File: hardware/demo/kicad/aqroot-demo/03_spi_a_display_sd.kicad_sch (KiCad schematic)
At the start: 21 parts, among them J1 FH69-50S-0.5SH, J2 Molex_5025700893, U17 TPS61169DCKR

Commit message: demo: the BOM is THREE QUARTERS orderable -- 122 part identities grafted from prior CTO audits, every one re-read off the PART instead of the line, and four gates that had never been run (D-614)
NO COPPER CHANGED.  The authoritative board is byte-identical at
c8e421aa50144fe396aedb5e226aaabeb815bd69ffaf6e04f549ded43831d103 and 26 of the
package's 28 artifacts are normalised-sha-identical to D-613's; the two that
moved are the two BOM views.

FAB7 coverage 25.9% -> 75.3%, orderable references 64 -> 186 of 247.
36 BOM lines / 122 references gained Manufacturer / MPN / LCSC -- 487 properties
across nine schematic sheets, replayable to byte-identical sheets.

Four things the mechanical answer would have got wrong: a REJECTED audit row's
JLC Manufacturer column names the match that was THROWN OUT (16 of 31 grafts);
the rating belongs to the PART, not the line; the designator is not the
identity; and the beta-dm 0 ohm current gate had never been run on five of the
Demo's eight links.

Two defects in the instruments fixed: the value parser could not read 15mR, and
MANIFEST.json hashed only the ROOT schematic sheet while nine child sheets
changed.

Re-proved on this tree: verify_promotion.py 14/14, FAB1-FAB6 + FAB8 PASS,
POP1-POP4, P1-P4, protected copper 15 nets / 393 objects IDENTICAL.
FAB7 still FAILS and is partitioned: 8 lines / 16 parts TUNE, 26 lines /
45 parts genuinely open.

Co-Authored-By: Claude Opus 5 <noreply@anthropic.com>
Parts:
- C13, C14: LCSC (none) -> C14663; MPN (none) -> CC0603KRX7R9BB104; Manufacturer (none) -> YAGEO; Note_Sourcing (none) -> SOURCING D-614. EXACT_PRIOR from the beta-dm audit line '10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
- C15: LCSC (none) -> C440198; MPN (none) -> GRM21BR61H106KE43L; Manufacturer (none) -> Murata Electronics; Note_Sourcing (none) -> SOURCING D-614. EXACT_PRIOR from the beta-dm audit line '10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
- C43: LCSC (none) -> C1779; MPN (none) -> CL21A475KAQNNNE; Manufacturer (none) -> Samsung Electro-Mechanics; Note_Sourcing (none) -> SOURCING D-614. CONTAINED_PRIOR from the beta-dm audit line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
- C44: LCSC (none) -> C28323; MPN (none) -> CL21B105KBFNNNE; Manufacturer (none) -> Samsung Electro-Mechanics; Note_Sourcing (none) -> SOURCING D-614. EXACT_PRIOR from the beta-dm audit line '1u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
- C56: LCSC (none) -> C15849; MPN (none) -> CL10A105KB8NNNC; Manufacturer (none) -> Samsung Electro-Mechanics; Note_Sourcing (none) -> SOURCING D-614. EXACT_PRIOR from the beta-dm audit line '1u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
- R113: LCSC (none) -> C25803; MPN (none) -> 0603WAF1003T5E; Manufacturer (none) -> UNI-ROYAL(Uniroyal Elec); Note_Sourcing (none) -> SOURCING D-614. EXACT_PRIOR from the beta-dm audit line '10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
- R25, R26: LCSC (none) -> C25804; MPN (none) -> 0603WAF1002T5E; Manufacturer (none) -> UNI-ROYAL(Uniroyal Elec); Note_Sourcing (none) -> SOURCING D-614. EXACT_PRIOR from the beta-dm audit line '10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

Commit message: demo: the BOM is 100% ORDERABLE and the safety part was ordered in the WRONG PACKAGE -- 61 identities ruled against a live distributor record, and a screen that asks the C26 question of every line at once (D-615)
D-614 named this task and named what stopped it: D-096 binds -- a part number
configured from an ordering scheme is a hypothesis until a distributor record
confirms lifecycle and stock, and that session had none to read.  This one read
the JLCPCB catalogue 225 times and KEPT every answer, each stamped with the UTC
minute it was read.

NO COPPER CHANGED.  The authoritative board is byte-identical at
c8e421aa50144fe396aedb5e226aaabeb815bd69ffaf6e04f549ded43831d103.

FAB7 IS CLOSED.  Coverage 75.3% -> 100.0%, orderable 186 -> 247 of 247,
needs_a_sourcing_decision ZERO lines, and fab_package_contract.py reads
FAB1-FAB8 PASS for the first time.

THE FINDING.  screen_part_land_parity.py asks D-613's C26 question of every
sourced line at once against the catalogue's own package field: 119 lines carry
a code, 75 are comparable, 74 MATCH and U18 did not.  The land is MSOP-10; the
BOM ordered LTC4368IDD-1#PBF, and DD is DFN-10-EP(3x3) -- against D-099, which
locked LTC4368IMS-1#PBF under FBV2-PWR-002's "no bottom-terminated parts" on
the single most safety-critical component.  The cached library symbol AND the
project .kicad_sym both still carried it, with a Package field describing a DFN
beside a Footprint field already reading MSOP-10.  Corrected to
LTC4368IMS-1#TRPBF, LCSC C688401 -- the tape-and-reel order code of the
identical device, D-210's precedent, not an electrical change.

Three things the obvious answer would have got wrong: R69 is 1.87 ohm and its
part is 0603WAF187KT5E while 0603WAF1873T5E is 187 kOhm; R95's node over-bound
UNDERSTATES its dissipation because a reversed cell adds in series (154 mW vs
54 mW); and R24/C12's Value strings are looser than their own symbol notes.
NET_MAX_DC grew 17 -> 48 established nodes to give the new dissipation gate
nu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
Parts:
- J1: LCSC (none) -> C25955556; Note_Sourcing (none) -> SOURCING D-615 LIVE_RECORD. The display FPC connector's LCS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
- R69: LCSC (none) -> C422967; MPN (none) -> 0603WAF187KT5E; Manufacturer (none) -> UNI-ROYAL(Uniroyal Elec); Note_Sourcing (none) -> SOURCING D-615 LIVE_RECORD. JLCPCB record read 2026-09-05T0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
- R70, R71, R72, R73: LCSC (none) -> C23140; MPN (none) -> 0603WAF330JT5E; Manufacturer (none) -> UNI-ROYAL(Uniroyal Elec); Note_Sourcing (none) -> SOURCING D-615 LIVE_RECORD. JLCPCB record read 2026-09-05T0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

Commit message: demo: D-750 and D-751 -- the external first-spin review found four real defects, and finishing its repairs found two more.
An external first-spin review (Fable 5.1 + Astra) reopened DEMO_READY_FOR_FAB at
b593b97 and named thirteen items.  Four were real defects on the frozen package:
J5's BOM identity still named the 2x12 BCS-112-S-D-HE that D-237 superseded eight
months ago, U14.6 QSTRT was physically floating behind a deliberate no_connect,
audit_rail_ampacity.py computed at 0.0174 mm inner copper against a board that
declares 0.0152 mm, and neither boost converter had a local input capacitor --
the nearest was 36.6 mm and the *named* input part 93.5 mm away.  A fifth,
item 7, is a design-condition failure: TI guarantees the TPS61169 OFF only when
the LED array's minimum Vf exceeds the maximum VIN, this panel is 2.9-3.2 V on a
3.3 V rail, and the shutdown DC path converges at about 25 mA -- a fifth of full
brightness, with no firmware mitigation because +3V3 is switched by SW9.

D-750 closed all of them and dispositioned the other nine, item by item, with
FIRST-ARTICLE and PROCUREMENT work explicitly separated from pre-order blockers.
The charger input was re-laid 250.8 -> 189.8 mm and 440 -> 216 mOhm, which is
what buys the 360 min tMAXCHG its margin; C83 and C84 were fitted on the existing
C33/C64 BOM line; Q11, the backlight true-off disconnect, was fitted on Q1's line.

D-751 FINISHED THE TRANSACTION, AND EACH THING IT TOUCHED HELD ANOTHER DEFECT.

* Q11 was on the board as a symbol and a BOM line and NOT as a circuit: three
  unapproved open edges, all three of them its own pins.  Routed with three
  --tap-first taps, 16.26 mm and four barrels.  The first run was REFUSED for a
  0.44 mm dangling In2 stub the tap left past its T; trimmed, re-run clean.
* placement_contract.py HAD NO WORD FOR AN ADDED PART, so the whole standing
  suite read "placement FAIL" for a legitimate act.  --add exists; PL7 now holds
  an ADDED pad to the same foreign-copper clearance a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
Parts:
- added Q11: AO3400A, Package_TO_SOT_SMD:SOT-23, symbol Transistor_FET:Q_NMOS_GSD
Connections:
- net DISP_BL_CTL: now also Q11.1 (G)
- net LED_K: now also Q11.2 (S); no longer J1.2 (LEDK), J1.3 (LEDK)
- new net LED_K_PANEL: J1.2 (LEDK), J1.3 (LEDK), Q11.3 (D)
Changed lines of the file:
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@@
 		)
 	)
-	(label "LED_K"
+	(label "LED_K_PANEL"
 		(at 59.69 120.65 180)
 		(effects
@@
 		)
 	)
-	(label "LED_K"
+	(label "LED_K_PANEL"
 		(at 59.69 123.19 180)
 		(effects
@@
 		(at 241.3 162.56 0)
 		(unit 1)
+		(body_style 1)
 		(exclude_from_sim no)
-		(in_bom no)
+		(in_bom yes)
 		(on_board yes)
+		(in_pos_files yes)
 		(dnp no)
 		(fields_autoplaced yes)
 		(property "Reference" "#PWR141"
-			(at 241.3 162.56 0)
+			(at 241.3 168.91 0)
+			(hide yes)
+			(show_name no)
+			(do_not_autoplace no)
 			(effects
 				(font
@@
 		)
 		(property "Value" "GND"
-			(at 241.3 162.56 0)
+			(at 241.3 167.64 0)
+			(show_name no)
+			(do_not_autoplace no)
 			(effects
 				(font
@@
 			(at 241.3 162.56 0)
 			(hide yes)
+			(show_name no)
+			(do_not_autoplace no)
 			(effects
 				(font
@@
 			(at 241.3 162.56 0)
 			(hide yes)
+			(show_name no)
+			(do_not_autoplace no)
 			(effects
 				(font
@@
 			)
 		)
-		(property "Description" "Power symbol"
+		(property "Description" "Power symbol creates a global label with name \"GND\" , ground"
 			(at 241.3 162.56 0)
 			(hide yes)
+			(show_name no)
+			(do_not_autoplace no)
 			(effects
 				(font
@@
 		(instances
 			(project "aqroot-Beta-v2"
-				(path "/e5ed7088-6df5-494c-ba15-bb4f5334a2b1"
+				(path "/8a0ad1ee-a49e-4cff-9a78-44823e373405/e86f9f15-4a7f-4160-bee2-09febc1b0776"
 					(reference "#PWR141")
 					(unit 1)
@@
 		)
 	)
+	(symbol
+		(lib_id "Transistor_FET:Q_NMOS_GSD")
+		(at 241.3 200.66 0)
+		(unit 1)
+		(body_style 1)
+		(exclude_from_sim no)
+		(in_bom yes)
+		(on_board yes)
+		(in_pos_files yes)
+		(dnp no)
+		(fields_autoplaced yes)
+		(property "Reference" "Q11"
+			(at 247.65 199.39 0)
+			(show_name no)
+			(do_not_autoplace no)
+			(effects
+				(font
+					(size 1.27 1.27)
+				)
+				(justify left)
+			)
+		)
+		(property "Value" "AO3400A"
+			(at 247.65 201.93 0)
+			(show_name no)
+			(do_not_autoplace no)
+			(effects
+				(font
+					(size 1.27 1.27)
+				)
+				(justify left)
+			)
+		)
+		(property "Footprint" "Package_TO_SOT_SMD:SOT-23"
+			(at 247.65 203.2 0)
+			(hide yes)
+			(show_name no)
+			(do_not_autoplace no)
+			(effects
+				(font
+					(size 1.27 1.27)
+				)
+			)
+		)
+		(property "Datasheet" ""
+			(at 241.3 200.66 0)
+			(hide yes)
+			(show_name no)
+			(do_not_autoplace no)
+			(effects
+				(font
+					(size 1.27 1.27)
+				)
+			)
+		)
+		(property "LCSC" "C20917"
+			(at 241.3 200.66 0)
+			(hide yes)
+			(show_name no)
+			(do_not_autoplace no)
+			(effects
+				(font
+					(size 1.27 1.27)
+				)
+			)
+		)
+		(property "Note_Sourcing" "SOURCING D-751 2026-09-18. The AO3400A was the ONLY line on the assembly BOM with no distributor identity (121 of 122 rows carried one), and D-750 made it a two-piece line by adding Q11, the display-backlight true-off disconnect. Verified live 2026-09-18 per D-096 through the JLCPCB parts API; record committed at evidence/jlc-live/ao3400a-568c27aa.json: LCSC C20917, Alpha & Omega Semicon, AO3400A, SOT-23, componentLibraryType = BASE (no extended-part fee, no feeder setup), stock 812570, 0.0847 USD at 1 / 0.0479 at 6000, 30 V, Id 5.7 A continuous, RDS(on) 48 mOhm at VGS 2.5 V, VGS(th) 1.45 V, Pd 1.4 W, -55 to +150 C, RoHS. BOTH FITTED USES ARE FAR INSIDE THAT ENVELOPE: Q1 sinks the IR LED and Q11 carries the 109 mA panel backlight cathode return, where even the worst-case 48 mOhm at a 2.5 V gate costs 5.2 mV. Stock is a snapshot, not a guarantee."
+			(at 241.3 200.66 0)
+			(hide yes)
+			(show_name no)
+			(do_not_autoplace no)
+			(effects
+				(font
+					(size 1.27 1.27)
+				)
+			)
+		)
+		(property "Manufacturer" "Alpha & Omega Semiconductor"
+			(at 241.3 200.66 0)
+			(hide yes)
+			(show_name no)
+			(do_not_autoplace no)
+			(effects
+				(font
+					(size 1.27 1.27)
+				)
+			)
+		)
+		(property "MPN" "AO3400A"
+			(at 241.3 200.66 0)
+			(hide yes)
+			(show_name no)
+			(do_not_autoplace no)
+			(effects
+				(font
+					(size 1.27 1.27)
+				)
+			)
+		)
+		(property "Package" "SOT-23-3, pin 1 = G, 2 = S, 3 = D (confirmed from the AOS datasheet)"
+			(at 241.3 200.66 0)
+			(hide yes)
+			(show_name no)
+			(do_not_autoplace no)
+			(effects
+				(font
+					(size 1.27 1.27)
+				)
+			)
+		)
+		(property "Note" "D-750 BACKLIGHT TRUE-OFF DISCONNECT.  TPS61169 (U17) shutdown does NOT make the panel dark: TI states a DC path remains from VIN through L3 and D8 to the LED string and guarantees OFF only when the LED array MINIMUM forward voltage exceeds the MAXIMUM VIN.  This board boosts from +3V3 and the EastRising ER-TFT035IPS-6 backlight is SIX LEDs IN PARALLEL at 2.9-3.2 V (D-079), so Vf(min) 2.9 V is BELOW the 3.3 V rail and the condition FAILS.  Solving the as-built network (+3V3 - L3 - D8 - R70..R73 8.25 R - six parallel LEDs - R69 1.87 R - GND) with a white-LED forward curve converges at about 25 mA: roughly a fifth of full brightness, plainly visible in a dark room, and about 82 mW of continuous drain whenever +3V3 is up and the backlight is commanded off.  +3V3 is switched by SW9, not by firmware, so there is no software mitigation: the screen would never go dark while the device is on.  Q11 breaks that DC path in the PANEL CATHODE RETURN, between J1 and the LED_K sense node.  IT IS OUTSIDE THE SENSE LOOP BY CONSTRUCTION: U17 LED pin and R69 both sit on Q11 SOURCE, so U17 still regulates exactly I = 200 mV / R69 and Q11 RDS(on) costs only headroom -- at the AO3400A's worst published 48 mOhm at VGS 2.5 V (LCSC C20917, verified live 2026-09-18) that is 5.2 mV at 109 mA, and the gate here is driven to 3.3 V, so the real figure is lower still; the boost makes it up.  THE LED CURRENT SETPOINT IS THEREFORE UNCHANGED at 109 mA typ / 100.5-117.6 mA over the VREF band (D-079), against the panel 120 mA maximum.  GATE IS DISP_BL_CTL, THE SAME SIGNAL THAT ENABLES U17, AND D-751 RECORDS THAT THIS IS A DESIGN CONSTRAINT AND NOT A CONVENIENCE.  PWM on this line shuts the converter down AND opens Q11 TOGETHER, which is the safe combination.  THE UNSAFE ONE IS CONVERTER-SWITCHING-WITH-Q11-OFF: an open LED path drives the TPS61169 output to its overvoltage clamp near 38 V, that node is the panel anode, and the panel cathode -- Q11 DRAIN -- follows it to within the string's sub-threshold drop, while Q11 SOURCE is held at 0 V by R69.  THE AO3400A IS A 30 V PART, so that combination would exceed VDS(max).  It cannot occur on this board because one net drives both gates: whenever U17 switches, Q11 is on and its VDS is the RDS(on) drop; whenever Q11 is off, U17 is in shutdown and the drain sits a few volts below the 3.3 V rail.  ANY FUTURE REVISION THAT SEPARATES THE TWO CONTROLS IN ORDER TO PWM Q11 ALONE MUST RE-RATE Q11 TO AT LEAST 40 V VDS.  SAFE OFF STATE IS PROVEN, NOT ASSUMED: R108 is a 10 k pull-down on DISP_BL_CTL_STRAP and R109 is a 0 R link, so the gate is held low during boot, reset, GPIO high-impedance and firmware crash; in the off state the DRAIN (panel side) is the higher potential so the body diode is reverse-biased, and AO3400A IDSS is under 1 uA at these voltages.  U17 LED pin is pulled to 0 V by R69 whenever Q11 is off, which is the safest of the two series positions.  SAME BOM LINE AS Q1: AO3400A, SOT-23, 1 = G, 2 = S, 3 = D, verified against AOS Rev 3.1 at FBV2-S1-007; this adds one piece to an existing line and creates no new purchasing identity."
+			(at 241.3 200.66 0)
+			(hide yes)
+			(show_name no)
+			(do_not_autoplace no)
+			(effects
+				(font
+					(size 1.27 1.27)
+				)
+			)
+		)
+		(property "Description" "N-MOSFET transistor, gate/source/drain"
+			(at 241.3 200.66 0)
+			(hide yes)
+			(show_name no)
+			(do_not_autoplace no)
+			(effects
+				(font
+					(size 1.27 1.27)
+				)
+			)
+		)
+		(pin "1"
+		)
+		(pin "2"
+		)
+		(pin "3"
+		)
+		(instances
+			(project "aqroot-Beta-v2"
+				(path "/8a0ad1ee-a49e-4cff-9a78-44823e373405/e86f9f15-4a7f-4160-bee2-09febc1b0776"
+					(reference "Q11")
+					(unit 1)
+				)
+			)
+		)
+	)
+	(wire
+		(pts
+			(xy 236.22 200.66) (xy 228.60000000000002 200.66)
+		)
+		(stroke
+			(width 0)
+			(type default)
+		)
+	)
+	(label "DISP_BL_CTL"
+		(at 228.60000000000002 200.66 180)
+		(effects
+			(font
+				(size 1.27 1.27)
+			)
+			(justify right bottom)
+		)
+	)
+	(wire
+		(pts
+			(xy 243.84 195.58) (xy 243.84 191.77)
+		)
+		(stroke
+			(width 0)
+			(type default)
+		)
+	)
+	(label "LED_K_PANEL"
+		(at 243.84 191.77 0)
+		(effects
+			(font
+				(size 1.27 1.27)
+			)
+			(justify left bottom)
+		)
+	)
+	(wire
+		(pts
+			(xy 243.84 205.74) (xy 243.84 209.55)
+		)
+		(stroke
+			(width 0)
+			(type default)
+		)
+	)
+	(label "LED_K"
+		(at 243.84 209.55 0)
+		(effects
+			(font
+				(size 1.27 1.27)
+			)
+			(justify left bottom)
+		)
+	)

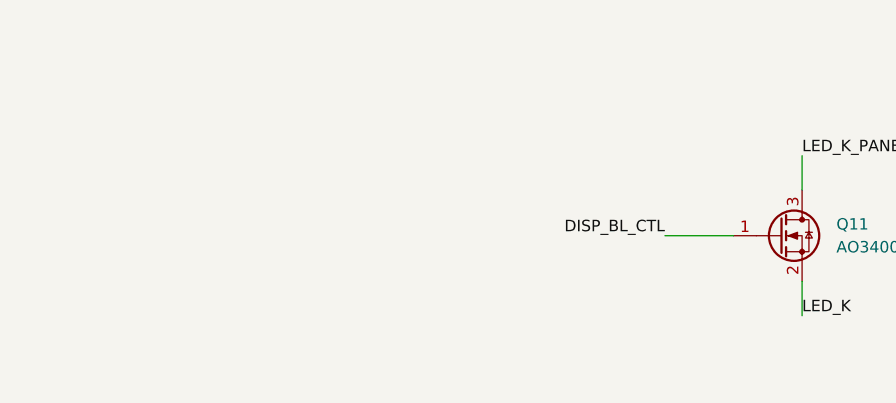
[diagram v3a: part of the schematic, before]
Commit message: demo: D-752 -- the backlight disconnect could not share the PWM pin, and the TPS61169 datasheet said so all along.
An independent CTO re-review held the D-751 DEMO_READY_FOR_FAB on one named
pre-order blocker: Q11, the backlight true-off disconnect D-750 fitted, had its
gate on /DISP_BL_CTL -- the same net as U17's CTRL.  D-751 had noticed that and
recorded it as a SAFETY CONSTRAINT.  The primary source says the opposite.

TI SNVSA40B 6.3.5: the TPS61169 "chops up the internal 204mV reference voltage
at the duty cycle of the PWM signal", filters it, and therefore "only the WLED
DC current is modulated, which is often referred as analog dimming".  CTRL is an
ANALOG dimming input; the converter keeps switching through every PWM low phase
and enters shutdown only after CTRL is low for longer than tSD, 2.5 ms MAX.  So
the shared gate created the forbidden state on every dimmed frame rather than on
none of them: FB below the 30 mV open-LED threshold, SW at VOVP_SW (36/37.5/39
V), 6.3.2 latching the part off after three switching cycles, and Q11's DRAIN --
the panel cathode -- at about 36 V while R69 holds its SOURCE at 0 V.  The
AO3400A is a 30 V part, and the firmware already drives ledcSetup(5000, 8) on
GPIO46.  The first brightness ramp would have latched the backlight off and
over-stressed Q11 on a board where every identity gate passed.

THE REPAIR IS STRUCTURAL, NOT PROCEDURAL.  The review proposed a separate static
enable from a spare U3 bit plus a documented sequence; that is a firmware promise
on a one-shot board, and one mis-sequence is the same 36 V across the same 30 V
part.  Q11's gate instead moved to its own net BL_DISC_G carrying the ENVELOPE of
DISP_BL_CTL: D14 (1N4148WS, LCSC C2128, JLCPCB BASIC, the SOD-323 land the board
already carries) charges C85 (100 nF) in about 25 us against U17's 6.5 ms
soft-start, and R132 (220 k) discharges it with tau = 22 ms.  Q11 cannot open
before 11.4 ms at worst-case tolerance while U17 is in shutdown by 2.5 ms --
4.6x,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
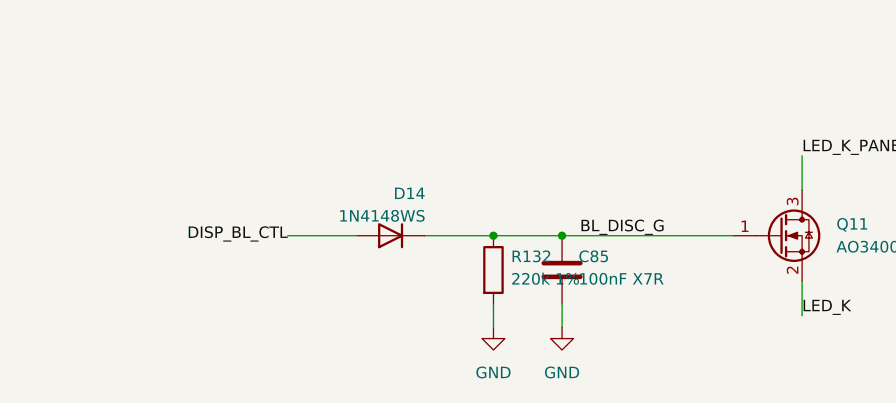
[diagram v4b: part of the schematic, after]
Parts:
- added C85: 100nF X7R, Capacitor_SMD:C_0603_1608Metric, symbol Device:C
- added D14: 1N4148WS, Diode_SMD:D_SOD-323, symbol Device:D
- added R132: 220k 1%, Resistor_SMD:R_0603_1608Metric, symbol Device:R
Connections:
- net DISP_BL_CTL: now also D14.2 (A); no longer Q11.1 (G)
- net GND: now also C85.2, R132.2
- new net BL_DISC_G: C85.1, D14.1 (K), Q11.1 (G), R132.1
